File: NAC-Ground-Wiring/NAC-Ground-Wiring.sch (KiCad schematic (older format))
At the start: 6 parts

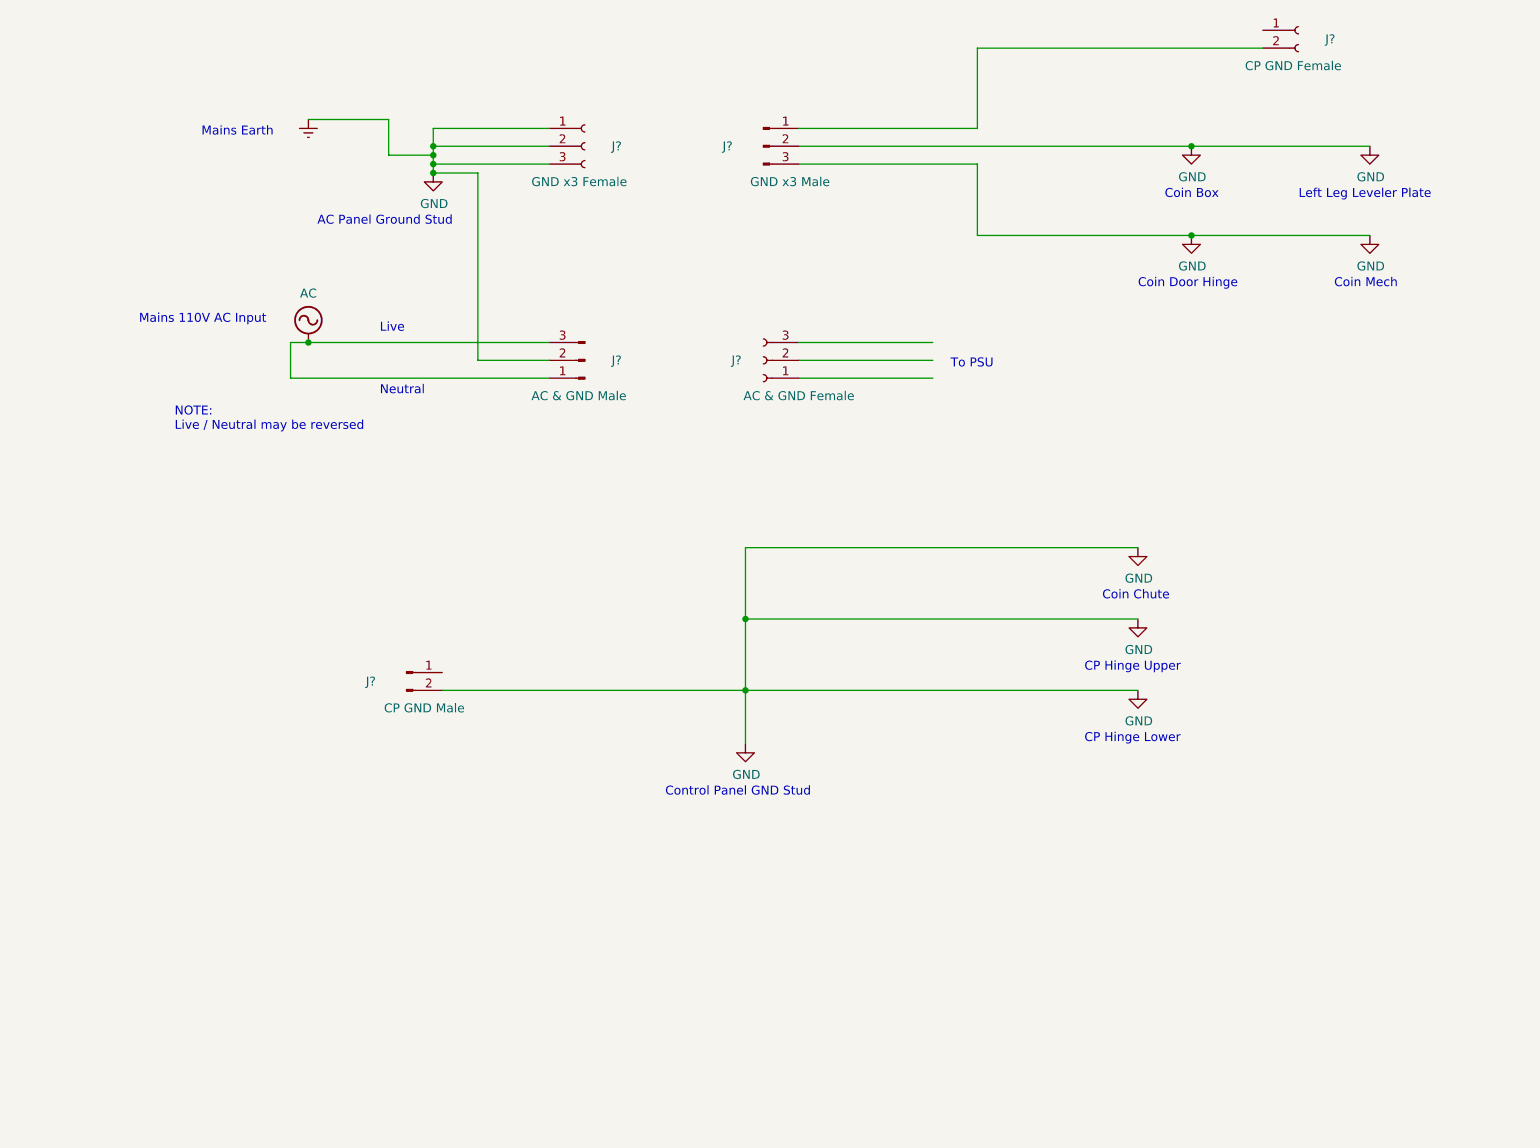
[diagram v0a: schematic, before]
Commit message: Updated to V1.1 based on found Sega diagram
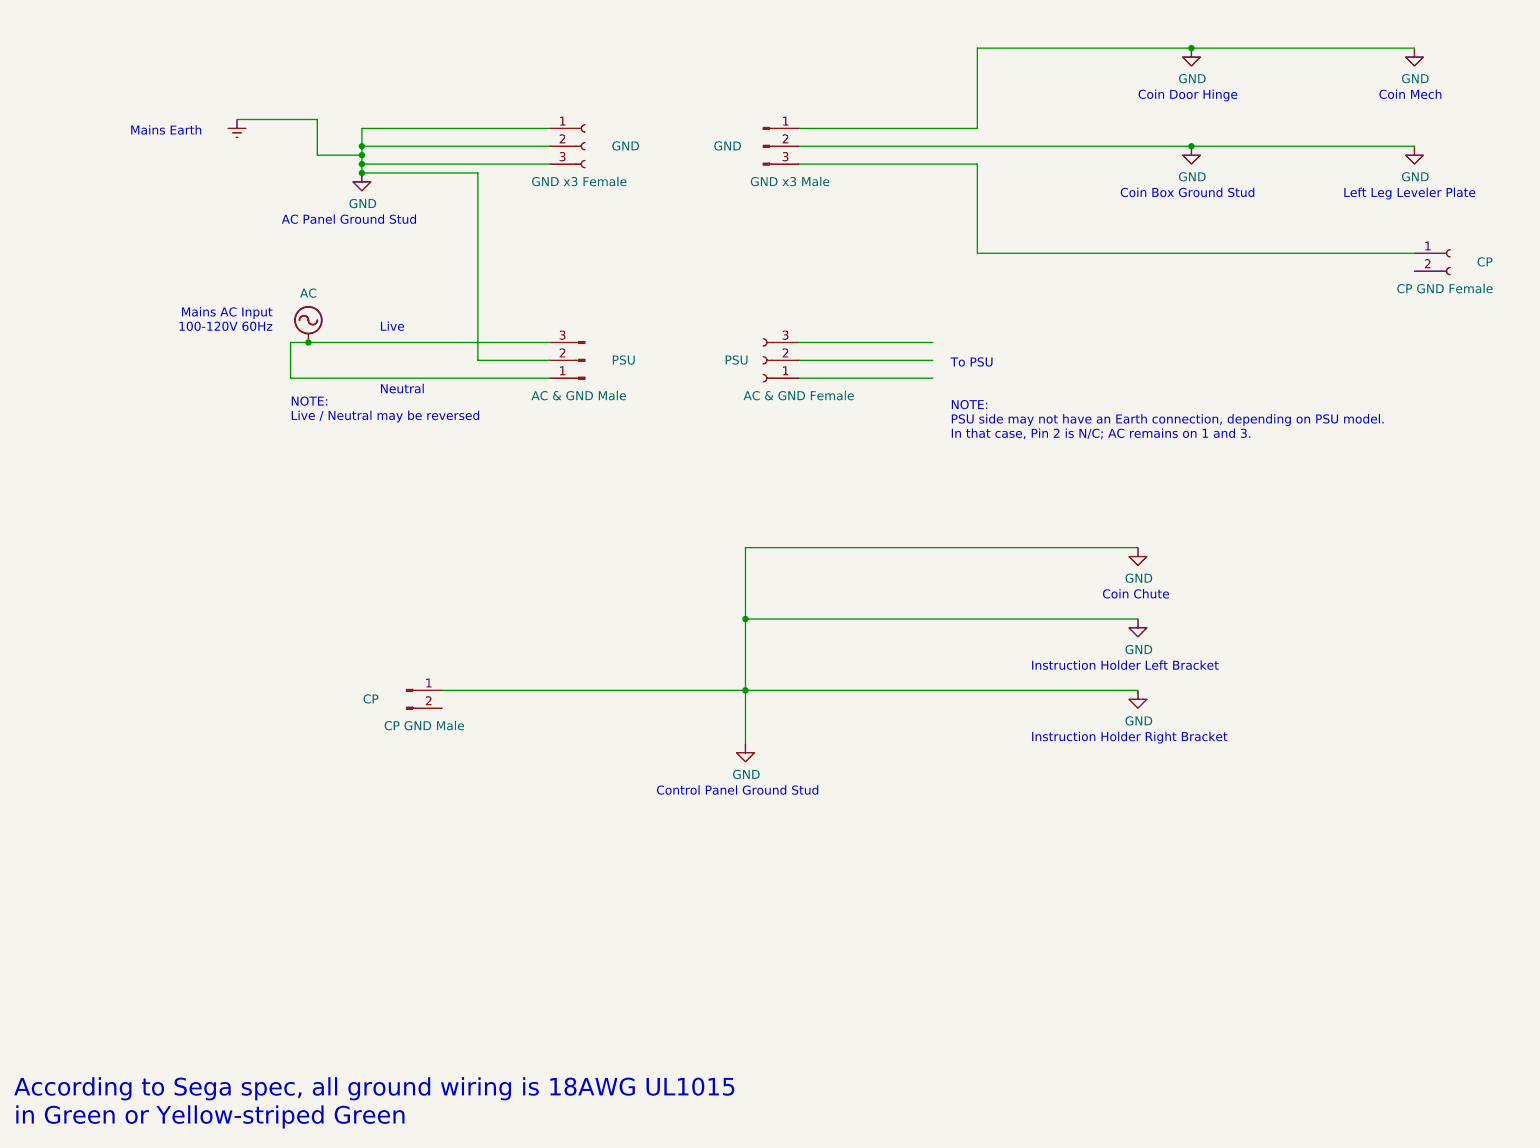
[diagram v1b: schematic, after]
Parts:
- gave numbers to parts that had none: 3
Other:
- note added: "According to Sega spec, all ground wiring is 18AWG UL1015 \nin Green or Yellow-striped Green"
- note added: "Coin Box Ground Stud"
- note added: "Control Panel Ground Stud"
- note added: "Instruction Holder Left Bracket"
- note added: "Instruction Holder Right Bracket"
- note added: "Mains AC Input\n100-120V 60Hz"
- note added: "NOTE:\nPSU side may not have an Earth connection, depending on PSU model.\nIn that case, Pin 2 is N/C; AC remains on 1 and 3."
- note removed: "CP Hinge Lower"
- note removed: "CP Hinge Upper"
- note removed: "Coin Box"
- note removed: "Control Panel GND Stud"
- note removed: "Mains 110V AC Input"
- moved on the sheet: CP
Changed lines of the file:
@@
 Title "New Astro City Ground Wiring"
 Date "2020-12-21"
-Rev "1.0"
+Rev "1.1"
 Comp "Softdrink 117"
 Comment1 ""
-Comment2 "I'm not sure if this matches the 'canonical' ground layout as originally designed."
-Comment3 "Diagram of current ground wiring connections in my Sega New Astro City arcade cabinet."
+Comment2 "Updated based on official Sega wiring diagrams."
+Comment3 "Diagram of earth ground wiring connections in a Sega New Astro City arcade cabinet."
 Comment4 ""
 $EndDescr
@@
 L power:Earth #PWR?
 U 1 1 5FBB4508
-P 2350 1950
-F 0 "#PWR?" H 2350 1700 50  0001 C CNN
-F 1 "Earth" H 2350 1800 50  0001 C CNN
-F 2 "" H 2350 1950 50  0001 C CNN
-F 3 "~" H 2350 1950 50  0001 C CNN
-	1    2350 1950
-	1    0    0    -1
-$EndComp
-Wire Wire Line
-	2350 1950 2800 1950
+P 1950 1950
+F 0 "#PWR?" H 1950 1700 50  0001 C CNN
+F 1 "Earth" H 1950 1800 50  0001 C CNN
+F 2 "" H 1950 1950 50  0001 C CNN
+F 3 "~" H 1950 1950 50  0001 C CNN
+	1    1950 1950
+	1    0    0    -1
+$EndComp
+Wire Wire Line
+	1950 1950 2400 1950
 Wire Wire Line
 	3300 3300 3700 3300
 $Comp
-L Connector:Conn_01x03_Female J?
+L Connector:Conn_01x03_Female GND
 U 1 1 5FBB67D4
 P 3900 2100
-F 0 "J?" H 4050 2100 50  0000 L CNN
+F 0 "GND" H 4050 2100 50  0000 L CNN
 F 1 "GND x3 Female" H 3600 1900 50  0000 L CNN
 F 2 "" H 3900 2100 50  0001 C CNN
@@
 $EndComp
 $Comp
-L Connector:Conn_01x03_Male J?
+L Connector:Conn_01x03_Male GND
 U 1 1 5FBBCEB0
 P 4900 2100
-F 0 "J?" H 4700 2100 50  0000 C CNN
+F 0 "GND" H 4700 2100 50  0000 C CNN
 F 1 "GND x3 Male" H 5050 1900 50  0000 C CNN
 F 2 "" H 4900 2100 50  0001 C CNN
@@
 $EndComp
 $Comp
-L Connector:Conn_01x03_Female J?
+L Connector:Conn_01x03_Female PSU
 U 1 1 5FBBD800
 P 4900 3300
-F 0 "J?" H 5050 3300 50  0000 C CNN
+F 0 "PSU" H 5050 3300 50  0000 C CNN
 F 1 "AC & GND Female" H 4700 3500 50  0000 C CNN
 F 2 "" H 4900 3300 50  0001 C CNN
@@
 L power:GND #PWR?
 U 1 1 5FBC3F75
-P 8300 2100
-F 0 "#PWR?" H 8300 1850 50  0001 C CNN
-F 1 "GND" H 8305 1927 50  0000 C CNN
-F 2 "" H 8300 2100 50  0001 C CNN
-F 3 "" H 8300 2100 50  0001 C CNN
-	1    8300 2100
-	1    0    0    -1
-$EndComp
-$Comp
-L Connector:Conn_01x02_Female J?
+P 8550 2100
+F 0 "#PWR?" H 8550 1850 50  0001 C CNN
+F 1 "GND" H 8555 1927 50  0000 C CNN
+F 2 "" H 8550 2100 50  0001 C CNN
+F 3 "" H 8550 2100 50  0001 C CNN
+	1    8550 2100
+	1    0    0    -1
+$EndComp
+$Comp
+L Connector:Conn_01x02_Female CP
 U 1 1 5FBC4BBE
-P 7900 1450
-F 0 "J?" H 8050 1400 50  0000 L CNN
-F 1 "CP GND Female" H 7600 1250 50  0000 L CNN
-F 2 "" H 7900 1450 50  0001 C CNN
-F 3 "~" H 7900 1450 50  0001 C CNN
-	1    7900 1450
+P 8750 2700
+F 0 "CP" H 8900 2650 50  0000 L CNN
+F 1 "CP GND Female" H 8450 2500 50  0000 L CNN
+F 2 "" H 8750 2700 50  0001 C CNN
+F 3 "~" H 8750 2700 50  0001 C CNN
+	1    8750 2700
 	1    0    0    -1
 $EndComp
@@
 L power:GND #PWR?
 U 1 1 5FBC6F48
-P 3050 2250
-F 0 "#PWR?" H 3050 2000 50  0001 C CNN
-F 1 "GND" H 3055 2077 50  0000 C CNN
-F 2 "" H 3050 2250 50  0001 C CNN
-F 3 "" H 3050 2250 50  0001 C CNN
-	1    3050 2250
-	1    0    0    -1
-$EndComp
-Wire Wire Line
-	2800 1950 2800 2150
-Wire Wire Line
-	2800 2150 3050 2150
-Wire Wire Line
-	3050 2200 3700 2200
-Wire Wire Line
-	3050 2150 3050 2200
-Wire Wire Line
-	3050 2150 3050 2100
-Wire Wire Line
-	3050 2100 3700 2100
-Connection ~ 3050 2150
-Wire Wire Line
-	3300 2250 3050 2250
-Wire Wire Line
-	3050 2250 3050 2200
-Connection ~ 3050 2250
-Connection ~ 3050 2200
-$Comp
-L Connector:Conn_01x03_Male J?
+P 2650 2250
+F 0 "#PWR?" H 2650 2000 50  0001 C CNN
+F 1 "GND" H 2655 2077 50  0000 C CNN
+F 2 "" H 2650 2250 50  0001 C CNN
+F 3 "" H 2650 2250 50  0001 C CNN
+	1    2650 2250
+	1    0    0    -1
+$EndComp
+Wire Wire Line
+	2400 1950 2400 2150
+Wire Wire Line
+	2400 2150 2650 2150
+Wire Wire Line
+	2650 2150 2650 2200
+Wire Wire Line
+	2650 2150 2650 2100
+Connection ~ 2650 2150
+Wire Wire Line
+	2650 2250 2650 2200
+Connection ~ 2650 2250
+Connection ~ 2650 2200
+$Comp
+L Connector:Conn_01x03_Male PSU
 U 1 1 5FBB72F5
 P 3900 3300
-F 0 "J?" H 3750 3300 50  0000 R CNN
+F 0 "PSU" H 3750 3300 50  0000 R CNN
 F 1 "AC & GND Male" H 4200 3500 50  0000 R CNN
 F 2 "" H 3900 3300 50  0001 C CNN
@@
 $EndComp
 Connection ~ 2350 3200
-Text Notes 2400 2550 0    50   ~ 0
+Text Notes 2200 2550 0    50   ~ 0
 AC Panel Ground Stud
 Wire Wire Line
 	3300 2250 3300 3300
-Text Notes 1400 3100 0    50   ~ 0
-Mains 110V AC Input
-Text Notes 1750 2050 0    50   ~ 0
+Text Notes 2150 3150 2    50   ~ 0
+Mains AC Input\n100-120V 60Hz
+Text Notes 1350 2050 0    50   ~ 0
 Mains Earth
 Wire Wire Line
@@
 Wire Wire Line
 	5100 2200 6100 2200
-Wire Wire Line
-	6100 1550 7700 1550
 $Comp
 L power:GND #PWR?
@@
 Text Notes 6800 4650 0    50   ~ 0
 Coin Chute
-Text Notes 6700 5050 0    50   ~ 0
-CP Hinge Upper
-Text Notes 6700 5450 0    50   ~ 0
-CP Hinge Lower
-Text Notes 4350 5750 0    50   ~ 0
-Control Panel GND Stud
+Text Notes 6400 5050 0    50   ~ 0
+Instruction Holder Left Bracket
+Text Notes 6400 5450 0    50   ~ 0
+Instruction Holder Right Bracket
+Text Notes 4300 5750 0    50   ~ 0
+Control Panel Ground Stud
 Wire Wire Line
 	4800 5450 4800 5150
@@
 	4800 5150 4800 4750
 Wire Wire Line
-	3050 2000 3050 2100
-Wire Wire Line
-	3050 2000 3700 2000
-Connection ~ 3050 2100
+	2650 2000 2650 2100
+Connection ~ 2650 2100
 Text Notes 2750 3150 0    50   ~ 0
 Live
 Text Notes 2750 3500 0    50   ~ 0
 Neutral
+Wire Wire Line
+	5100 2100 7300 2100
+Text Notes 8350 1850 0    50   ~ 0
+Coin Mech
+$Comp
+L power:GND #PWR?
+U 1 1 5FBD3CF2
+P 8550 1550
+F 0 "#PWR?" H 8550 1300 50  0001 C CNN
+F 1 "GND" H 8555 1377 50  0000 C CNN
+F 2 "" H 8550 1550 50  0001 C CNN
+F 3 "" H 8550 1550 50  0001 C CNN
+	1    8550 1550
+	1    0    0    -1
+$EndComp
+Text Notes 7000 1850 0    50   ~ 0
+Coin Door Hinge
+Text Notes 6900 2400 0    50   ~ 0
+Coin Box Ground Stud
+Wire Wire Line
+	6100 1550 7300 1550
+$Comp
+L power:GND #PWR?
+U 1 1 5FBD159C
+P 7300 1550
+F 0 "#PWR?" H 7300 1300 50  0001 C CNN
+F 1 "GND" H 7305 1377 50  0000 C CNN
+F 2 "" H 7300 1550 50  0001 C CNN
+F 3 "" H 7300 1550 50  0001 C CNN
+	1    7300 1550
+	1    0    0    -1
+$EndComp
+Text Notes 8150 2400 0    50   ~ 0
+Left Leg Leveler Plate
+Wire Wire Line
+	5100 2000 6100 2000
+$Comp
+L Connector:Conn_01x02_Male CP
+U 1 1 5FE1C0D0
+P 2900 5150
+F 0 "CP" H 2700 5100 50  0000 C CNN
+F 1 "CP GND Male" H 3000 4950 50  0000 C CNN
+F 2 "" H 2900 5150 50  0001 C CNN
+F 3 "~" H 2900 5150 50  0001 C CNN
+	1    2900 5150
+	1    0    0    -1
+$EndComp
+Wire Wire Line
+	3100 5150 4800 5150
+Text Notes 2250 3650 0    50   ~ 0
+NOTE:\nLive / Neutral may be reversed
+Wire Wire Line
+	6100 2200 6100 2700
+Text Notes 5950 3750 0    50   ~ 0
+NOTE:\nPSU side may not have an Earth connection, depending on PSU model.\nIn that case, Pin 2 is N/C; AC remains on 1 and 3.
+Wire Wire Line
+	7300 1550 8550 1550
+Connection ~ 7300 1550
+Wire Wire Line
+	7300 2100 8550 2100
 Connection ~ 7300 2100
 Wire Wire Line
-	7300 2100 8300 2100
-Wire Wire Line
-	5100 2100 7300 2100
-Text Notes 8100 2900 0    50   ~ 0
-Coin Mech
-Connection ~ 7300 2600
-Wire Wire Line
-	7300 2600 8300 2600
-$Comp
-L power:GND #PWR?
-U 1 1 5FBD3CF2
-P 8300 2600
-F 0 "#PWR?" H 8300 2350 50  0001 C CNN
-F 1 "GND" H 8305 2427 50  0000 C CNN
-F 2 "" H 8300 2600 50  0001 C CNN
-F 3 "" H 8300 2600 50  0001 C CNN
-	1    8300 2600
-	1    0    0    -1
-$EndComp
-Text Notes 7000 2900 0    50   ~ 0
-Coin Door Hinge
-Text Notes 7150 2400 0    50   ~ 0
-Coin Box
-Wire Wire Line
-	6100 2600 7300 2600
-$Comp
-L power:GND #PWR?
-U 1 1 5FBD159C
-P 7300 2600
-F 0 "#PWR?" H 7300 2350 50  0001 C CNN
-F 1 "GND" H 7305 2427 50  0000 C CNN
-F 2 "" H 7300 2600 50  0001 C CNN
-F 3 "" H 7300 2600 50  0001 C CNN
-	1    7300 2600
-	1    0    0    -1
-$EndComp
-Text Notes 7900 2400 0    50   ~ 0
-Left Leg Leveler Plate
-Wire Wire Line
-	6100 2200 6100 2600
-Wire Wire Line
-	5100 2000 6100 2000
-$Comp
-L Connector:Conn_01x02_Male J?
-U 1 1 5FE1C0D0
-P 2900 5050
-F 0 "J?" H 2700 5000 50  0000 C CNN
-F 1 "CP GND Male" H 3000 4850 50  0000 C CNN
-F 2 "" H 2900 5050 50  0001 C CNN
-F 3 "~" H 2900 5050 50  0001 C CNN
-	1    2900 5050
-	1    0    0    -1
-$EndComp
-Wire Wire Line
-	3100 5150 4800 5150
-Text Notes 1600 3700 0    50   ~ 0
-NOTE:\nLive / Neutral may be reversed
+	6100 2700 8550 2700
+Wire Wire Line
+	2650 2250 3300 2250
+Wire Wire Line
+	2650 2200 3700 2200
+Wire Wire Line
+	2650 2100 3700 2100
+Wire Wire Line
+	2650 2000 3700 2000
+Text Notes 700  7600 0    98   ~ 0
+According to Sega spec, all ground wiring is 18AWG UL1015 \nin Green or Yellow-striped Green
 $EndSCHEMATC
